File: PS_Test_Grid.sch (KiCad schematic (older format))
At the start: 52 parts, among them J1 CONN_01X03, J10 CONN_01X01, J2 CONN_01X01, J3 CONN_01X01, J4 CONN_01X01, J5 CONN_01X01, J6 CONN_01X03, J7 CONN_01X01, J8 CONN_01X01, J9 CONN_01X01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

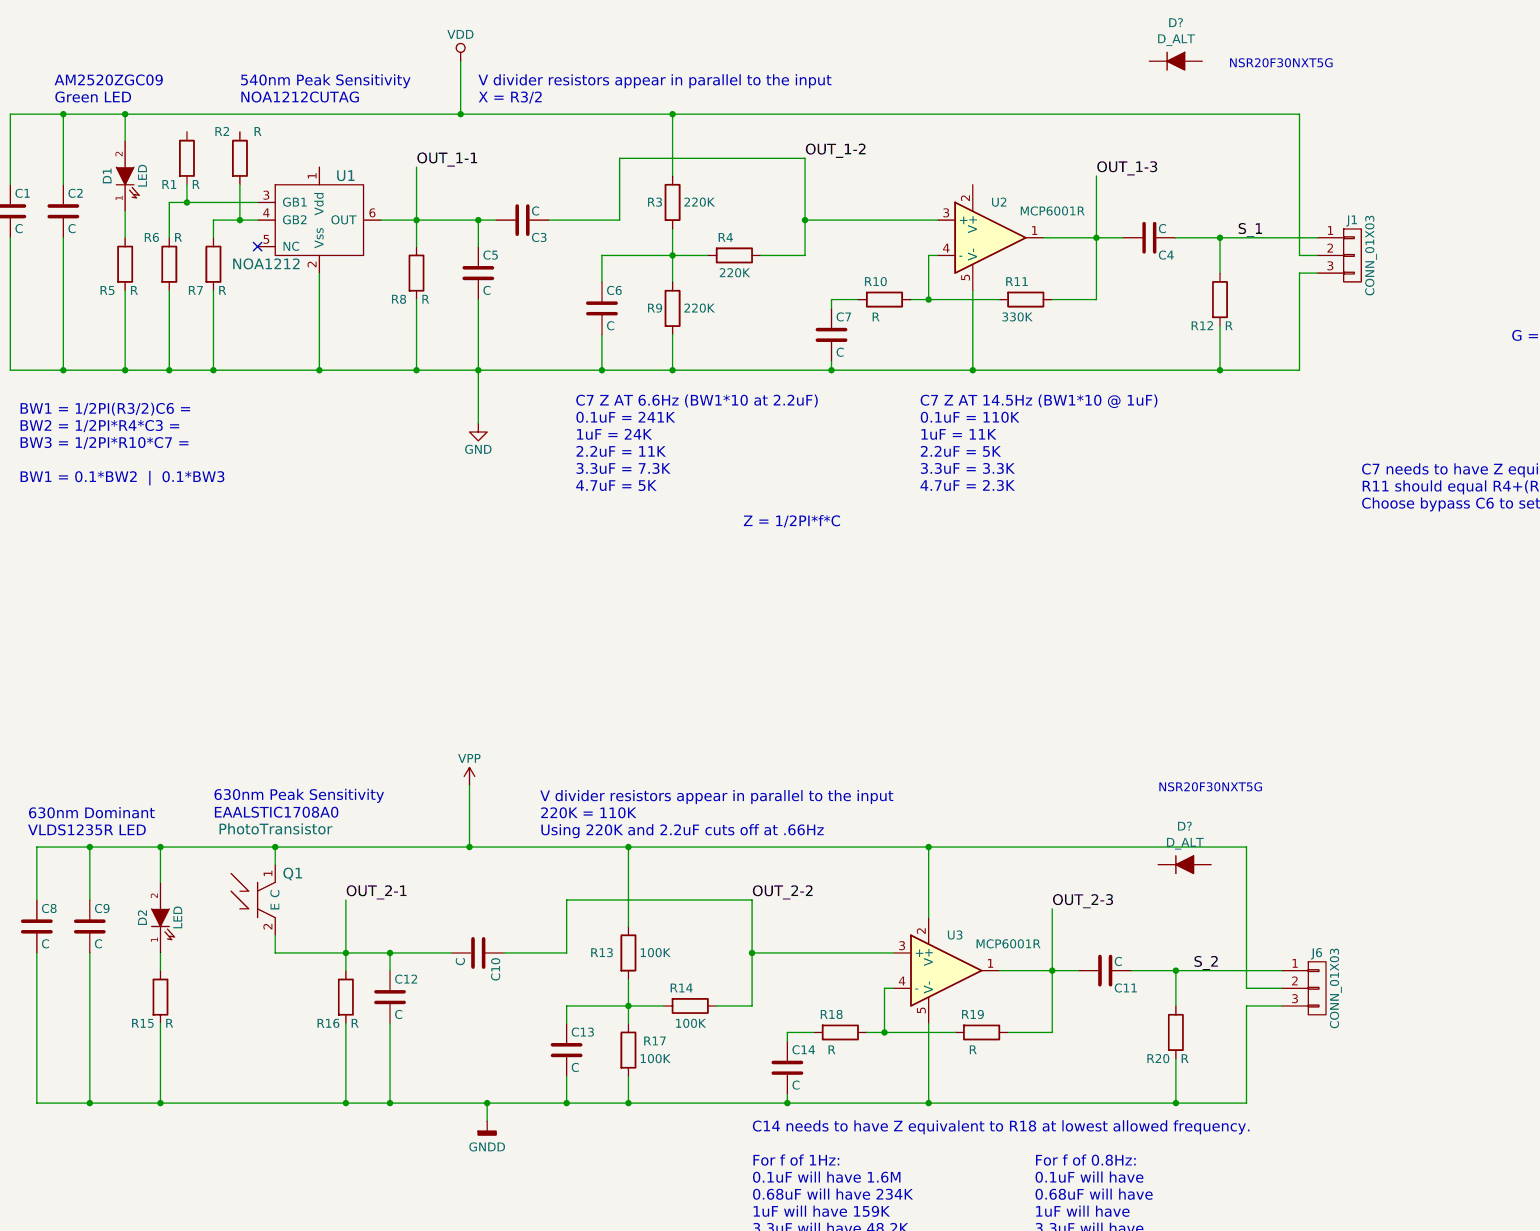
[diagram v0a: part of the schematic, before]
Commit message: laid out all drc pass
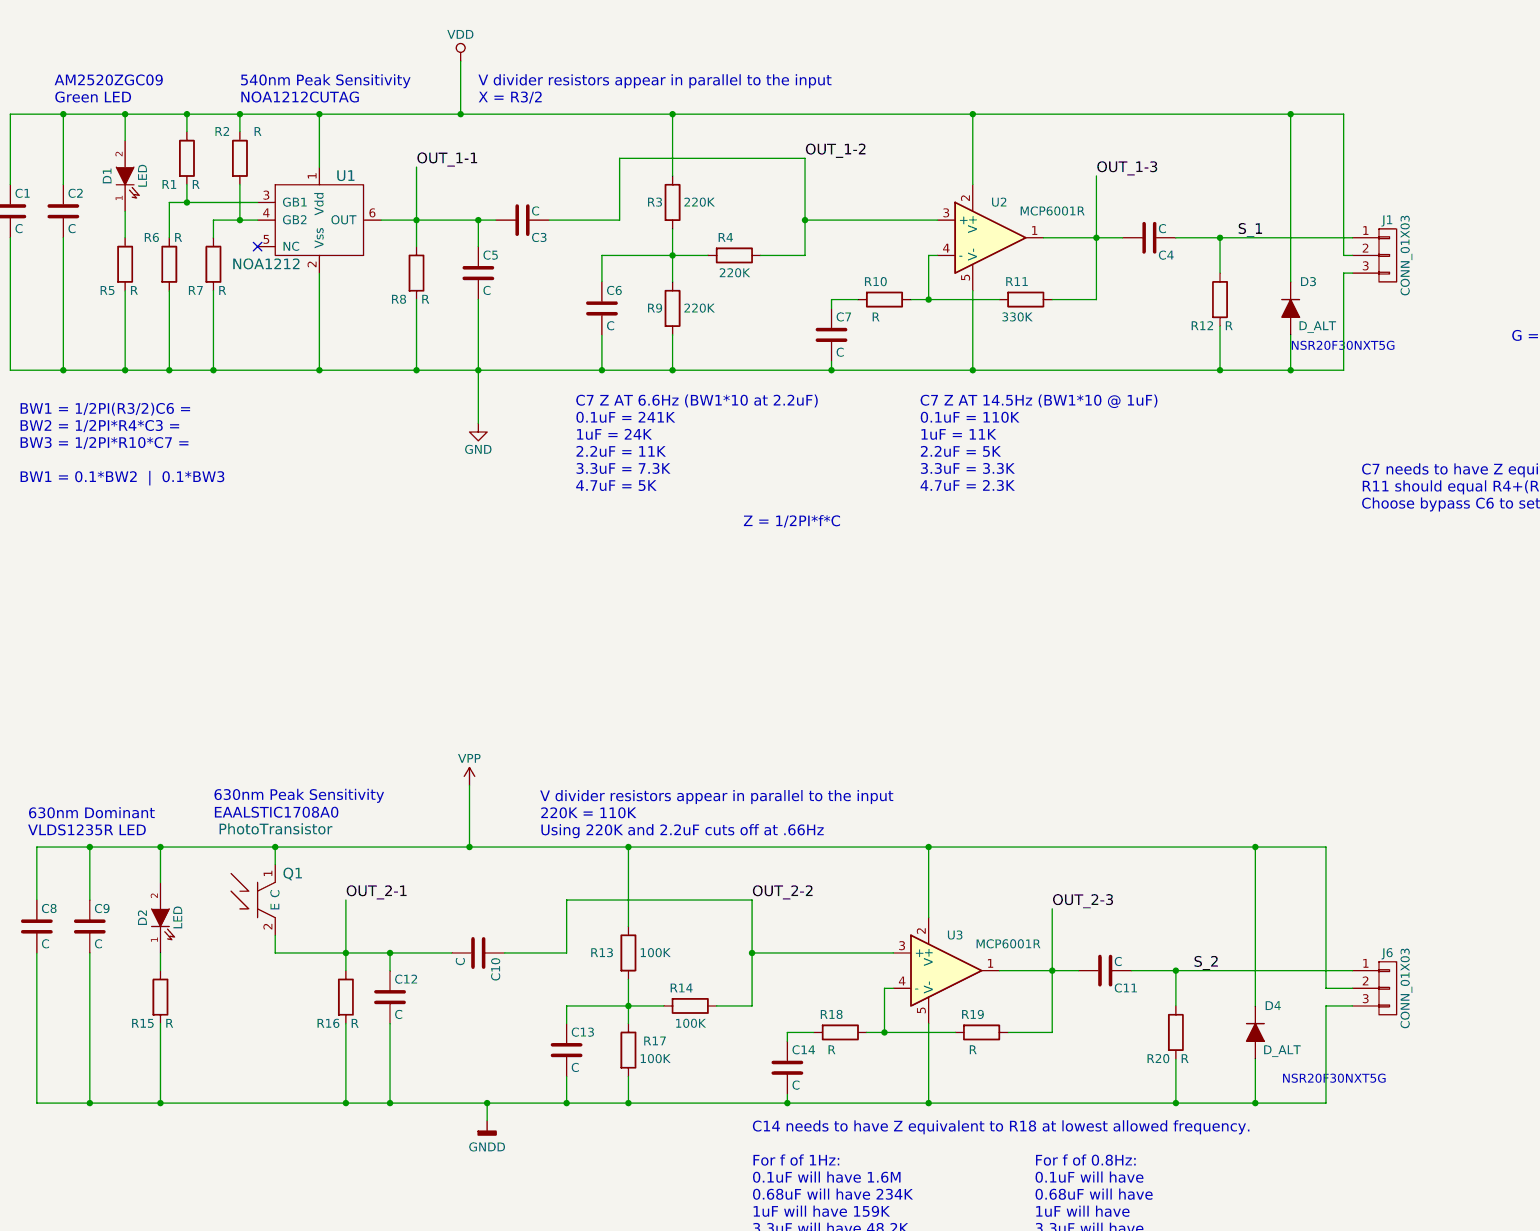
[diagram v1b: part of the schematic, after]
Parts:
- D3, D4: renamed from D?; footprint (none) -> Solutions:NSR20F30NXT5G_DIODE
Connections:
- net GND: now also D3.2 (A)
- net GNDD: now also D4.2 (A)
- net VDD: now also D3.1 (K), R1.1, R2.1, U1.1 (Vdd), U2.2 (V+)
- net VPP: now also D4.1 (K)
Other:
- moved on the sheet: D3, D4, J1, J6
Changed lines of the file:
@@
 L PS_Test_Grid-rescue:CONN_01X03 J1
 U 1 1 5B92B63C
-P 13000 2900
-F 0 "J1" H 13000 3100 50  0000 C CNN
-F 1 "CONN_01X03" V 13100 2900 50  0000 C CNN
-F 2 "Pin_Headers:Pin_Header_Straight_1x03_Pitch2.54mm" H 13000 2900 50  0001 C CNN
-F 3 "" H 13000 2900 50  0001 C CNN
-	1    13000 2900
+P 13200 2900
+F 0 "J1" H 13200 3100 50  0000 C CNN
+F 1 "CONN_01X03" V 13300 2900 50  0000 C CNN
+F 2 "Pin_Headers:Pin_Header_Straight_1x03_Pitch2.54mm" H 13200 2900 50  0001 C CNN
+F 3 "" H 13200 2900 50  0001 C CNN
+	1    13200 2900
 	1    0    0    -1
 $EndComp
@@
 L PS_Test_Grid-rescue:CONN_01X03 J6
 U 1 1 5B92B762
-P 12800 7050
-F 0 "J6" H 12800 7250 50  0000 C CNN
-F 1 "CONN_01X03" V 12900 7050 50  0000 C CNN
-F 2 "Pin_Headers:Pin_Header_Straight_1x03_Pitch2.54mm" H 12800 7050 50  0001 C CNN
-F 3 "" H 12800 7050 50  0001 C CNN
-	1    12800 7050
+P 13200 7050
+F 0 "J6" H 13200 7250 50  0000 C CNN
+F 1 "CONN_01X03" V 13300 7050 50  0000 C CNN
+F 2 "Pin_Headers:Pin_Header_Straight_1x03_Pitch2.54mm" H 13200 7050 50  0001 C CNN
+F 3 "" H 13200 7050 50  0001 C CNN
+	1    13200 7050
 	1    0    0    -1
 $EndComp
 Wire Wire Line
-	12600 7150 12400 7150
-Wire Wire Line
-	12400 7150 12400 7700
-Wire Wire Line
-	12400 7050 12600 7050
-Wire Wire Line
-	12400 6250 12400 7050
-Wire Wire Line
-	12800 2900 12700 2900
-Wire Wire Line
-	12800 3000 12700 3000
-Wire Wire Line
-	12700 3550 12700 3000
+	13000 7150 12850 7150
+Wire Wire Line
+	12850 7150 12850 7700
+Wire Wire Line
+	12850 7050 13000 7050
+Wire Wire Line
+	12850 6250 12850 7050
+Wire Wire Line
+	13000 2900 12950 2900
+Wire Wire Line
+	13000 3000 12950 3000
+Wire Wire Line
+	12950 3550 12950 3000
 $Comp
 L PS_Test_Grid-rescue:CONN_01X01 J2
@@
 Connection ~ 9600 6850
 Wire Wire Line
-	12700 2900 12700 2100
+	12950 2900 12950 2100
 Connection ~ 12250 2800
 Connection ~ 12250 3550
@@
 	9600 6850 9600 7150
 Wire Wire Line
-	12250 2800 12800 2800
-Wire Wire Line
-	12250 3550 12700 3550
-Wire Wire Line
-	12000 7700 12400 7700
-Wire Wire Line
-	12000 6950 12600 6950
-$Comp
-L Device:D_ALT D?
+	12250 2800 13000 2800
+Wire Wire Line
+	12250 3550 12650 3550
+Wire Wire Line
+	12000 7700 12450 7700
+Wire Wire Line
+	12000 6950 13000 6950
+$Comp
+L Device:D_ALT D3
 U 1 1 5BFF69DD
-P 12000 1800
-F 0 "D?" H 12000 2016 50  0000 C CNN
-F 1 "D_ALT" H 12000 1925 50  0000 C CNN
-F 2 "" H 12000 1800 50  0001 C CNN
-F 3 "~" H 12000 1800 50  0001 C CNN
-	1    12000 1800
-	1    0    0    -1
-$EndComp
-$Comp
-L Device:D_ALT D?
+P 12650 3200
+F 0 "D3" V 12500 3300 50  0000 C CNN
+F 1 "D_ALT" V 12750 3350 50  0000 C CNN
+F 2 "Solutions:NSR20F30NXT5G_DIODE" H 12650 3200 50  0001 C CNN
+F 3 "~" H 12650 3200 50  0001 C CNN
+	1    12650 3200
+	0    1    1    0
+$EndComp
+$Comp
+L Device:D_ALT D4
 U 1 1 5BFF6A6F
-P 12050 6350
-F 0 "D?" H 12050 6566 50  0000 C CNN
-F 1 "D_ALT" H 12050 6475 50  0000 C CNN
-F 2 "" H 12050 6350 50  0001 C CNN
-F 3 "~" H 12050 6350 50  0001 C CNN
-	1    12050 6350
-	1    0    0    -1
-$EndComp
-Wire Wire Line
-	9150 2100 12700 2100
-Wire Wire Line
-	6050 2100 7950 2100
+P 12450 7300
+F 0 "D4" V 12300 7400 50  0000 C CNN
+F 1 "D_ALT" V 12550 7450 50  0000 C CNN
+F 2 "Solutions:NSR20F30NXT5G_DIODE" H 12450 7300 50  0001 C CNN
+F 3 "~" H 12450 7300 50  0001 C CNN
+	1    12450 7300
+	0    1    1    0
+$EndComp
+Wire Wire Line
+	9150 2100 10850 2100
+Wire Wire Line
+	6050 2100 6400 2100
 Wire Wire Line
 	6250 6250 6250 6450
 Wire Wire Line
-	10600 6250 12400 6250
+	10600 6250 12450 6250
 Wire Wire Line
 	8900 6250 10600 6250
@@
 Wire Wire Line
 	5700 2100 6050 2100
-Text Notes 11900 5950 0    50   ~ 0
+Text Notes 12600 7600 0    50   ~ 0
 NSR20F30NXT5G
-Text Notes 12300 1850 0    50   ~ 0
+Text Notes 12650 3450 0    50   ~ 0
 NSR20F30NXT5G
+Wire Wire Line
+	6400 2200 6400 2100
+Connection ~ 6400 2100
+Wire Wire Line
+	6400 2100 6700 2100
+Wire Wire Line
+	6700 2200 6700 2100
+Connection ~ 6700 2100
+Wire Wire Line
+	6700 2100 7150 2100
+Wire Wire Line
+	7150 2400 7150 2100
+Connection ~ 7150 2100
+Wire Wire Line
+	7150 2100 7950 2100
+Wire Wire Line
+	10850 2500 10850 2100
+Connection ~ 10850 2100
+Wire Wire Line
+	10850 2100 12650 2100
+Wire Wire Line
+	12650 3050 12650 2100
+Connection ~ 12650 2100
+Wire Wire Line
+	12650 2100 12950 2100
+Wire Wire Line
+	12650 3350 12650 3550
+Connection ~ 12650 3550
+Wire Wire Line
+	12650 3550 12950 3550
+Wire Wire Line
+	12450 7150 12450 6250
+Connection ~ 12450 6250
+Wire Wire Line
+	12450 6250 12850 6250
+Wire Wire Line
+	12450 7450 12450 7700
+Connection ~ 12450 7700
+Wire Wire Line
+	12450 7700 12850 7700
 $EndSCHEMATC

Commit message: minor notes
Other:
- note added: "Don’t need C5 or C12 to cut 60Hz noise\nLikely don’t need output C or R"
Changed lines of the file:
@@
 Wire Wire Line
 	12450 7700 12850 7700
+Text Notes 6100 4700 0    50   ~ 0
+Don’t need C5 or C12 to cut 60Hz noise\nLikely don’t need output C or R
 $EndSCHEMATC
